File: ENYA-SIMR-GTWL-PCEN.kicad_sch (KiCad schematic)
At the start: 11 parts, among them J1 PICO_BLADE_1x6_MALE_RA_SMD, SW1 PEC11H-4015F-S0016

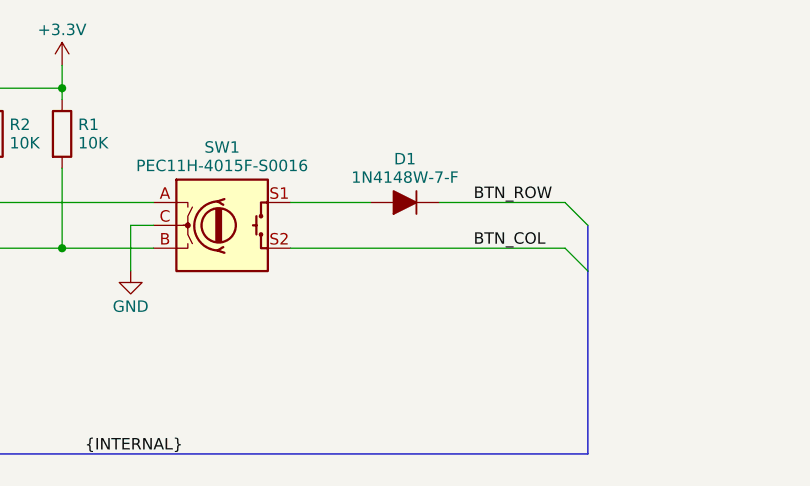
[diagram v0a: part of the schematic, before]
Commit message: correction button matrix diode polarity
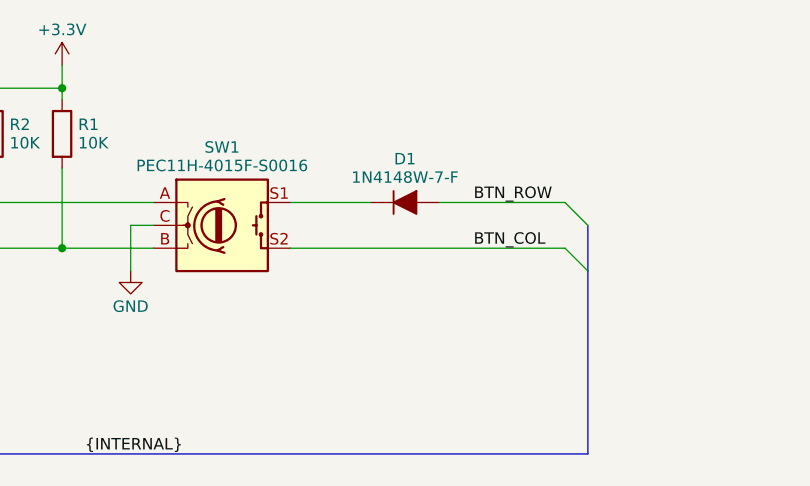
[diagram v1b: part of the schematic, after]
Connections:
- net BTN_ROW: now also D1.2 (A); no longer D1.1 (K)
- net at SW1.S1: now also D1.1 (K); no longer D1.2 (A)
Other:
- moved on the sheet: D1
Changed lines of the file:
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@@
     )
   )
-  (symbol (lib_id "ENYA_Diode_Rectifier:1N4148W-7-F_SOD-123") (at 248.92 129.54 180) (unit 1)
+  (symbol (lib_id "ENYA_Diode_Rectifier:1N4148W-7-F_SOD-123") (at 248.92 129.54 0) (unit 1)
     (in_bom yes) (on_board yes) (dnp no) (fields_autoplaced)
     (property "Reference" "D1" (at 248.92 124.7154 0)
@@
       (effects (font (size 1.27 1.27)))
     )
-    (property "Footprint" "Diode_SMD:D_SOD-123" (at 248.92 125.095 0)
+    (property "Footprint" "Diode_SMD:D_SOD-123" (at 248.92 133.985 0)
       (effects (font (size 1.27 1.27)) hide)
     )

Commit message: WIP
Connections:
- net +3.3V: now also J1.6 (Pin_6); no longer J1.1 (Pin_1)
- net BTN_COL: now also J1.5 (Pin_5); no longer J1.2 (Pin_2)
- net BTN_ROW: now also J1.4 (Pin_4); no longer J1.3 (Pin_3)
- net ENC_A: now also J1.3 (Pin_3); no longer J1.4 (Pin_4)
- net ENC_B: now also J1.2 (Pin_2); no longer J1.5 (Pin_5)
- net GND: now also J1.1 (Pin_1); no longer J1.6 (Pin_6)
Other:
- moved on the sheet: J1
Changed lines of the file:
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@@
     )
   )
-  (symbol (lib_id "ENYA_Connector_PicoBlade:PICO_BLADE_1x6_MALE_RA_SMD") (at 127 129.54 0) (mirror y) (unit 1)
-    (in_bom yes) (on_board yes) (dnp no) (fields_autoplaced)
-    (property "Reference" "J1" (at 127 119.61 0)
+  (symbol (lib_id "ENYA_Connector_PicoBlade:PICO_BLADE_1x6_MALE_RA_SMD") (at 127 132.08 180) (unit 1)
+    (in_bom yes) (on_board yes) (dnp no)
+    (property "Reference" "J1" (at 127 142.01 0)
       (effects (font (size 1.27 1.27)))
     )
-    (property "Value" "PICO_BLADE_1x6_MALE_RA_SMD" (at 127 139.7 0)
+    (property "Value" "PICO_BLADE_1x6_MALE_RA_SMD" (at 127 121.92 0)
       (effects (font (size 1.27 1.27)) hide)
     )
-    (property "Footprint" "ENYA_Connector_PicoBlade:PICO_BLADE_53261_1x6_SMD_RA_1.25MM" (at 127 127 0)
+    (property "Footprint" "ENYA_Connector_PicoBlade:PICO_BLADE_53261_1x6_SMD_RA_1.25MM" (at 127 134.62 0)
       (effects (font (size 1.27 1.27)) hide)
     )
-    (property "Datasheet" "https://tools.molex.com/pdm_docs/sd/532610671_sd.pdf" (at 127 129.54 0)
+    (property "Datasheet" "https://tools.molex.com/pdm_docs/sd/532610671_sd.pdf" (at 127 132.08 0)
       (effects (font (size 1.27 1.27)) hide)
     )
-    (property "Manufacturer" "Molex" (at 127 127 0)
+    (property "Manufacturer" "Molex" (at 127 134.62 0)
       (effects (font (size 1.27 1.27)) hide)
     )
-    (property "Manufacturer Part Number" "0532610671" (at 127 121.658 0)
+    (property "Manufacturer Part Number" "0532610671" (at 127 139.962 0)
       (effects (font (size 1.27 1.27)))
     )
-    (property "Digi-Key Part Number" "WM7624CT-ND" (at 127 129.54 0)
+    (property "Digi-Key Part Number" "WM7624CT-ND" (at 127 132.08 0)
       (effects (font (size 1.27 1.27)) hide)
     )
